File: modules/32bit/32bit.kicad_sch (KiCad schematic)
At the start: 19 parts, among them J5 USB_C_Receptacle_USB2.0_14P, SW1 K2-1808SN-A4SW-01, SW2 K2-1808SN-A4SW-01, U1 ESP32-S3-WROOM-1U-N16R8

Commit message: Add 32bit schematics
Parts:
- removed INPUT2: Conn_01x02_Socket, Connector_PinSocket_2.54mm:PinSocket_1x02_P2.54mm_Vertical, symbol Connector:Conn_01x02_Socket
- removed V1: 3.3, symbol Simulation_SPICE:VDC
- removed V2: VSIN, symbol Simulation_SPICE:VSIN
- added C21, C22, C26, C34, C36, C39: 0.1uf, Capacitor_SMD:C_0402_1005Metric, symbol Device:C_Small
- added C27, C33, C35, C37, C38, C5: 10uf, Capacitor_SMD:C_0402_1005Metric, symbol Device:C_Small
- added C6: 0.1uf, Capacitor_SMD:C_0402_1005Metric, symbol Device:C
- added D1: LED, LED_SMD:LED_0603_1608Metric, symbol Device:LED
- added R1, R2, R9: 1k, Resistor_SMD:R_0402_1005Metric, symbol Device:R
- added R10, R12: 100k, Resistor_SMD:R_0402_1005Metric, symbol Device:R
- added R13, R17: 1k, Resistor_SMD:R_0402_1005Metric, symbol Device:R_Small
- added R14, R18, R26, R7, R8: 33, Resistor_SMD:R_0402_1005Metric, symbol Device:R_Small
- added R24, R25: 4.7k, Resistor_SMD:R_0402_1005Metric, symbol Device:R_Small
- added R5, R6: 1.5k, Resistor_SMD:R_0402_1005Metric, symbol Device:R_Small
- added RV1, RV2: 50k, BreadModular_Pots:Potentiometer_RV09, symbol Device:R_Potentiometer
- added SW4: K2-1808SN-A4SW-01, BreadModular_MISC:K2-1808SN-A4SW-01, symbol Switch:SW_SPST
- added U3: MCP6002-xSN, Package_SO:SOIC-8-1EP_3.9x4.9mm_P1.27mm_EP2.29x3mm, symbol Amplifier_Operational:MCP6002-xSN
- added U4: ~, Package_DFN_QFN:QFN-28-1EP_4x4mm_P0.45mm_EP2.4x2.4mm_ThermalVias, symbol BreadModular_Symbols:ES8388
- INPUT1: value Conn_01x08_Socket -> Conn_01x05_Socket; footprint Connector_PinSocket_2.54mm:PinSocket_1x08_P2.54mm_Vertical -> Connector_PinSocket_2.54mm:PinSocket_1x05_P2.54mm_Vertical; symbol Connector:Conn_01x08_Socket -> Connector:Conn_01x05_Socket
- OUTPUT1: value Conn_01x08_Socket -> Conn_01x05_Socket; symbol Connector:Conn_01x08_Socket -> Connector:Conn_01x05_Socket
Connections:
- net GND: now also C21.2, C22.2, C26.2, C27.1, C33.2, C34.2, C35.2, C36.2, C37.2, C38.2, C39.2, C5.2, C6.2, R9.1, RV1.1, RV2.1, SW4.1 (A), U3.4 (V-), U4.13 (HPGND), U4.18 (AGND), U4.26 (CE), U4.29 (Thermal_Vias), U4.4 (DGND)
- net LED_MODE: now reaches U1.11 (IO18)
- net LED_MODE: now also D1.2 (A)
- net BUTTON_MODE: now reaches U1.12 (IO8)
- net BUTTON_MODE: now also SW4.2 (B)
- net CV1: now reaches U1.17 (IO9)
- net CV1: now also INPUT1.4 (Pin_4), R10.2, U3.3 (+)
- net CV2: now reaches U1.18 (IO10)
- net CV2: now also INPUT1.5 (Pin_5), R12.2, U3.5 (+)
- net at U1.19 (IO11): now also R7.2
- net at U1.20 (IO12): now also R8.2
- net at U1.21 (IO13): now also R14.2
- net at U1.22 (IO14): now also R18.2
- net at U1.23 (IO21): now also R26.1
- net CDATA: now reaches U1.24 (IO47)
- net CDATA: now also R24.1, U4.27 (CDATA)
- net CCLK: now reaches U1.25 (IO48)
- net CCLK: now also R25.1, U4.28 (CCLK)
- net at U1.38 (IO2): now also R2.2
- net at U1.39 (IO1): now also R1.2
- net EN: no longer names the net of C3.2, C4.2, R3.2, SW2.2 (B), U1.3 (EN)
- net IO0: no longer names the net of SW1.2 (B), U1.27 (IO0)
- net IO15: no longer names the net of U1.8 (IO15)
- net IO15: no longer INPUT1.6 (Pin_6)
- net IO16: no longer names the net of U1.9 (IO16)
- net IO16: no longer INPUT1.7 (Pin_7)
- net IO17: no longer names the net of U1.10 (IO17)
- net IO17: no longer INPUT1.8 (Pin_8)
- net IO35: no longer names the net of U1.28 (IO35)
- net IO35: no longer OUTPUT1.8 (Pin_8)
- net IO36: no longer names the net of U1.29 (IO36)
- net IO36: no longer OUTPUT1.7 (Pin_7)
- net IO37: no longer names the net of U1.30 (IO37)
- net IO37: no longer OUTPUT1.6 (Pin_6)
- net IO38: no longer names the net of U1.31 (IO38)
- net IO38: no longer OUTPUT1.5 (Pin_5)
- net IO39: no longer names the net of U1.32 (IO39)
- net IO39: no longer OUTPUT1.4 (Pin_4)
- net IO4: no longer names the net of U1.4 (IO4)
- net IO4: no longer INPUT1.2 (Pin_2)
- net IO40: no longer names the net of U1.33 (IO40)
- net IO40: no longer OUTPUT1.3 (Pin_3)
- net IO41: no longer names the net of U1.34 (IO41)
- net IO41: no longer OUTPUT1.2 (Pin_2)
- net IO5: no longer names the net of U1.5 (IO5)
- net IO5: no longer INPUT1.3 (Pin_3)
- net IO6: no longer names the net of U1.6 (IO6)
- net IO6: no longer INPUT1.4 (Pin_4)
- net IO7: no longer names the net of U1.7 (IO7)
- net IO7: no longer INPUT1.5 (Pin_5)
- new net: D1.1 (K), R9.2
- new net: R13.2, U4.11 (ROUT1)
- new net: R6.2, RV2.3
- new net: R5.2, RV1.3
- new net: R5.1, U3.1, U3.2 (-)
- new net: R6.1, U3.6 (-), U3.7
- new net: C33.1, C34.1, U4.20 (VMID)
- new net: R17.2, U4.12 (LOUT1)
- new net: C27.2, U4.10 (VREF)
- new net: C35.1, C36.1, U4.19 (ADCVREF)
- new net +3V3: C21.1, C22.1, C26.1, C37.1, C38.1, C39.1, C5.1, C6.1, R10.1, R12.1, R24.2, R25.2, U3.8 (V+), U4.16 (HPVDD), U4.17 (AVDD), U4.2 (DVDD), U4.3 (PVDD)
- new net AIN_1: INPUT1.2 (Pin_2), U4.24 (LIN1)
- new net AIN_2: INPUT1.3 (Pin_3), U4.23 (RIN1)
- new net AOUT_1: OUTPUT1.2 (Pin_2), R17.1
- new net AOUT_2: OUTPUT1.3 (Pin_3), R13.1
- new net ASDOUT: R26.2, U4.8 (ASDOUT)
- new net BUFF_CV1: RV1.2
- new net BUFF_CV2: RV2.2
- new net DSDIN: R18.1, U4.6 (DSDIN)
- new net GOUT_1: OUTPUT1.4 (Pin_4), R1.1
- new net GOUT_2: OUTPUT1.5 (Pin_5), R2.1
- new net LRCK: R14.1, U4.7 (LRCK)
- new net MCLK: R7.1, U4.1 (MCLK)
- new net SCLK: R8.1, U4.5 (SCLK)
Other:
- note added: "## Audio Codec ES8388"
- note added: "## CV_IN 1.5k before the pot is to reduce the voltage goes to ADC since we need to do some attenuation."
- note added: "## Other IO"
- note added: "## Processing Unit ESP32"
- note added: "## USB-C Setup"
- moved on the sheet: C20, GND1, J5, R11, R4, V_SUPPLY1

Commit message: Finished basic routing
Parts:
- OUTPUT1: footprint Connector_PinSocket_2.54mm:PinSocket_1x08_P2.54mm_Vertical -> Connector_PinSocket_2.54mm:PinSocket_1x05_P2.54mm_Vertical
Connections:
- net V_SUPPLY is gone; now on net +3V3: C1.1, C2.1, R3.1, U1.2 (3V3), V_SUPPLY1.1 (Pin_1), V_SUPPLY1.2 (Pin_2), V_SUPPLY1.3 (Pin_3), V_SUPPLY1.4 (Pin_4), V_SUPPLY1.5 (Pin_5)
- net ASDOUT: now also R7.1; no longer R26.2
- net BUFF_CV1: now also U1.17 (IO9)
- net BUFF_CV2: now also U1.18 (IO10)
- net CCLK: now also R24.1, U4.27 (CDATA); no longer R25.1, U4.28 (CCLK)
- net CDATA: now also R25.1, U4.28 (CCLK); no longer R24.1, U4.27 (CDATA)
- net CV1: no longer U1.17 (IO9)
- net CV2: no longer U1.18 (IO10)
- net DSDIN: now also R14.1; no longer R18.1
- net LRCK: now also R8.1; no longer R14.1
- net MCLK: now also R26.2; no longer R7.1
- net SCLK: now also R18.1; no longer R8.1

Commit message: Add the production files
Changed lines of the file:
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@@
-	(wire
-		(pts
-			(xy 80.01 86.36) (xy 81.28 86.36)
-		)
-		(stroke
-			(width 0)
-			(type default)
-		)
-	)
 	(wire
 		(pts
@@
 	(wire
 		(pts
-			(xy 80.01 109.22) (xy 81.28 109.22)
-		)
-		(stroke
-			(width 0)
-			(type default)
-		)
-	)
-	(wire
-		(pts
-			(xy 80.01 83.82) (xy 81.28 83.82)
-		)
-		(stroke
-			(width 0)
-			(type default)
-		)
-	)
-	(wire
-		(pts
 			(xy 224.79 54.61) (xy 228.6 54.61)
 		)
@@
 	(wire
 		(pts
-			(xy 80.01 111.76) (xy 81.28 111.76)
-		)
-		(stroke
-			(width 0)
-			(type default)
-		)
-	)
-	(wire
-		(pts
 			(xy 539.75 36.83) (xy 542.29 36.83)
 		)
@@
 	(wire
 		(pts
-			(xy 114.3 71.12) (xy 111.76 71.12)
-		)
-		(stroke
-			(width 0)
-			(type default)
-		)
-	)
-	(wire
-		(pts
 			(xy 128.27 245.11) (xy 128.27 251.46)
 		)
@@
 	(wire
 		(pts
-			(xy 80.01 88.9) (xy 81.28 88.9)
-		)
-		(stroke
-			(width 0)
-			(type default)
-		)
-	)
-	(wire
-		(pts
 			(xy 134.62 246.38) (xy 134.62 255.27)
 		)
@@
 		)
 		(stroke
-			(width 0)
-			(type default)
-		)
-	)
-	(wire
-		(pts
-			(xy 80.01 81.28) (xy 81.28 81.28)
-		)
-		(stroke

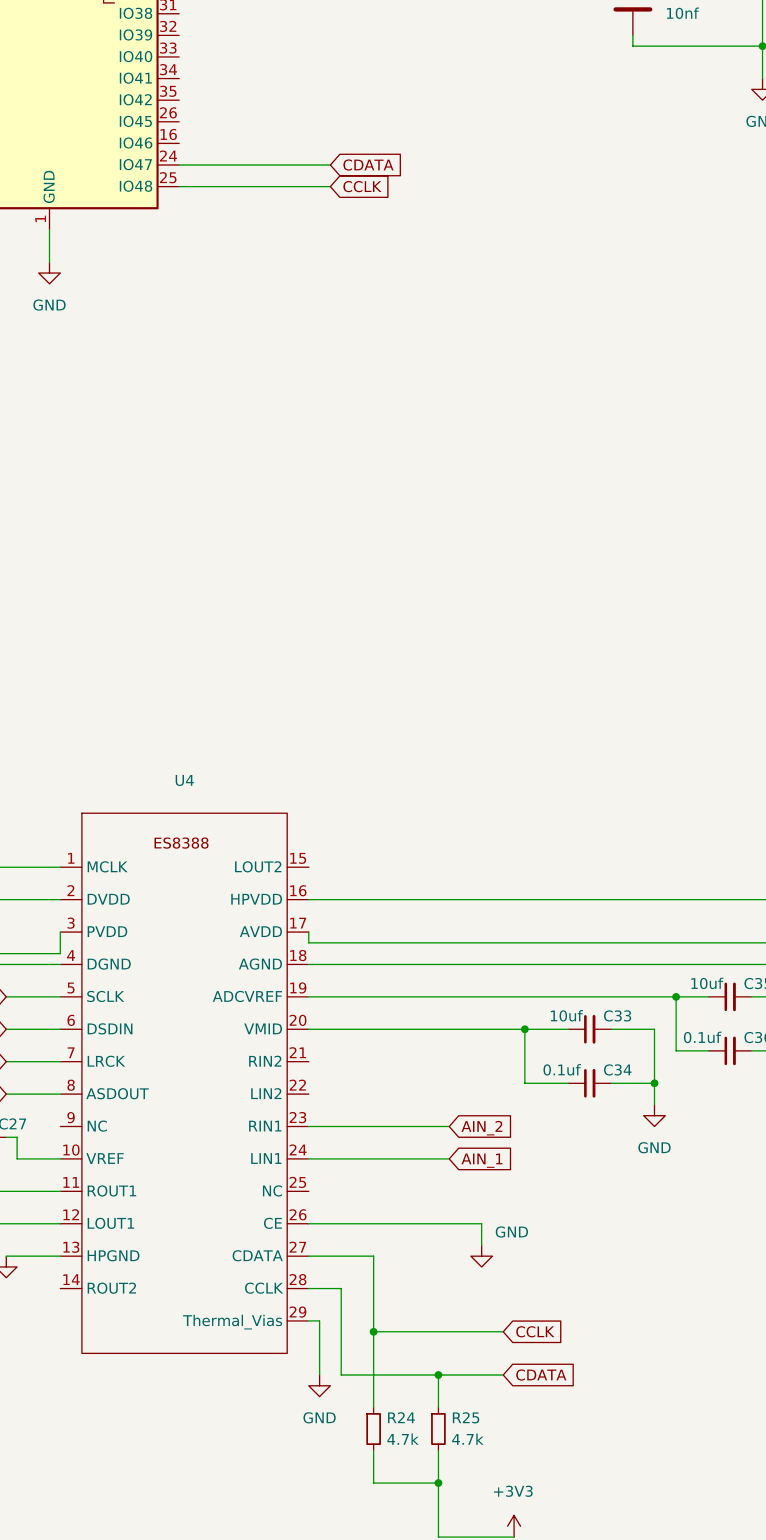
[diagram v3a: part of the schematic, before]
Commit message: 16bit: Moved CDATA & CCLK labels. They were just being marked wrongly in the ES8388 side
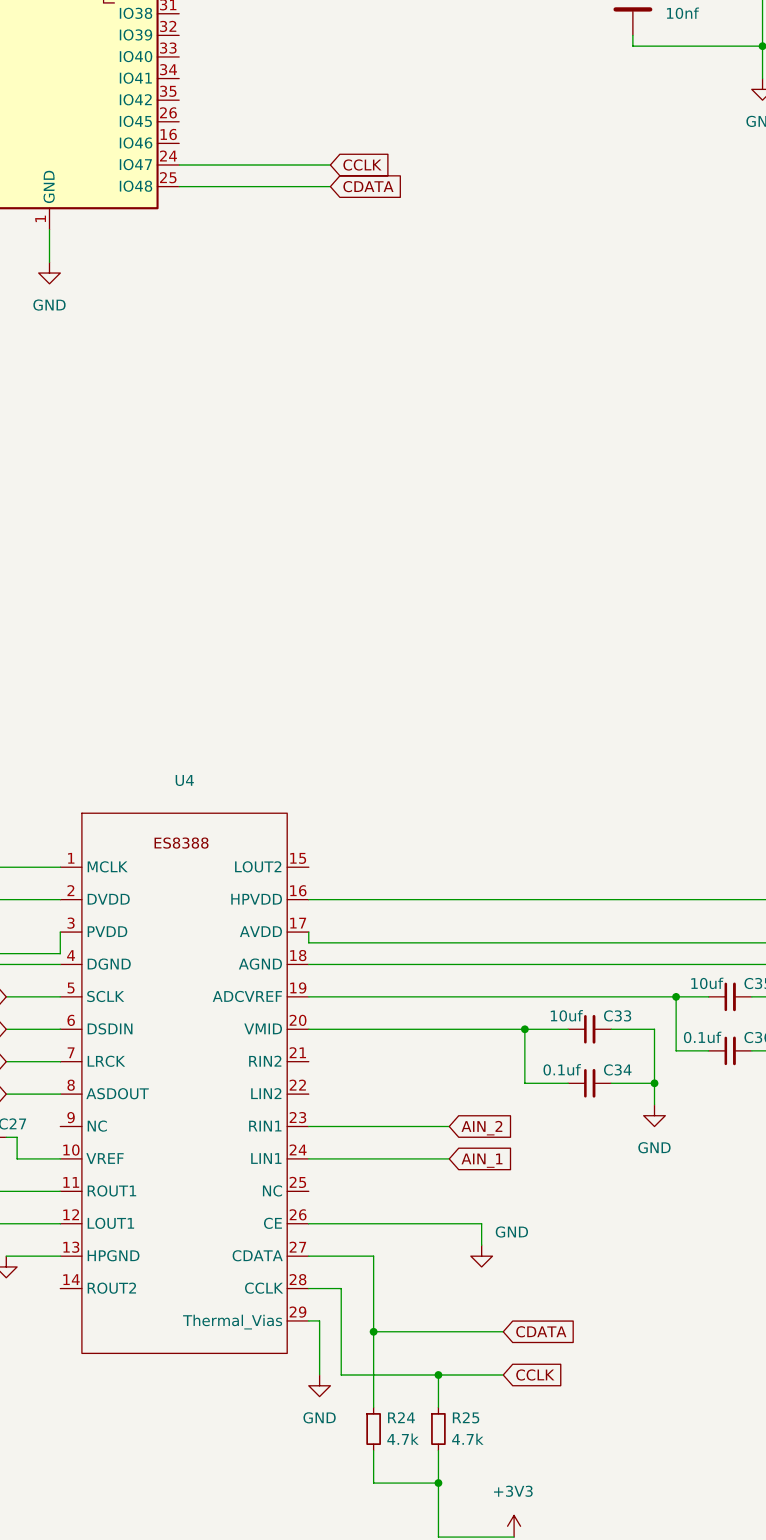
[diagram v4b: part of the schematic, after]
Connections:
- net CCLK: now also R25.1, U1.24 (IO47), U4.28 (CCLK); no longer R24.1, U1.25 (IO48), U4.27 (CDATA)
- net CDATA: now also R24.1, U1.25 (IO48), U4.27 (CDATA); no longer R25.1, U1.24 (IO47), U4.28 (CCLK)
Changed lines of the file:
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@@
 	)
 	(junction
+		(at 134.62 246.38)
+		(diameter 0)
+		(color 0 0 0 0)
+	)
+	(junction
 		(at 217.17 222.25)
 		(diameter 0)
@@
 	)
 	(junction
-		(at 134.62 246.38)
-		(diameter 0)
-		(color 0 0 0 0)
-	)
-	(junction
 		(at 506.73 38.1)
 		(diameter 0)
@@
 	)
 	(junction
-		(at 142.24 251.46)
-		(diameter 0)
-		(color 0 0 0 0)
-	)
-	(junction
 		(at 53.34 66.04)
 		(diameter 0)
@@
 		(color 0 0 0 0)
 	)
+	(junction
+		(at 142.24 251.46)
+		(diameter 0)
+		(color 0 0 0 0)
+	)
 	(wire
 		(pts
@@
 	(wire
 		(pts
-			(xy 142.24 251.46) (xy 149.86 251.46)
-		)
-		(stroke
-			(width 0)
-			(type default)
-		)
-	)
-	(wire
-		(pts
 			(xy 96.52 43.18) (xy 96.52 60.96)
 		)
@@
 	(wire
 		(pts
-			(xy 111.76 109.22) (xy 129.54 109.22)
+			(xy 33.02 307.34) (xy 48.26 307.34)
 		)
 		(stroke
@@
 	(wire
 		(pts
-			(xy 33.02 307.34) (xy 48.26 307.34)
+			(xy 116.84 311.15) (xy 116.84 309.88)
 		)
 		(stroke
@@
 	(wire
 		(pts
-			(xy 116.84 311.15) (xy 116.84 309.88)
+			(xy 127 233.68) (xy 147.32 233.68)
 		)
 		(stroke
@@
 	(wire
 		(pts
-			(xy 127 233.68) (xy 147.32 233.68)
+			(xy 111.76 109.22) (xy 129.54 109.22)
 		)
 		(stroke
@@
 	(wire
 		(pts
-			(xy 134.62 237.49) (xy 134.62 246.38)
-		)
-		(stroke
-			(width 0)
-			(type default)
-		)
-	)
-	(wire
-		(pts
 			(xy 91.44 218.44) (xy 97.79 218.44)
 		)
@@
 	(wire
 		(pts
+			(xy 134.62 246.38) (xy 134.62 255.27)
+		)
+		(stroke
+			(width 0)
+			(type default)
+		)
+	)
+	(wire
+		(pts
 			(xy 204.47 337.82) (xy 208.28 337.82)
 		)
@@
 	(wire
 		(pts
-			(xy 134.62 246.38) (xy 134.62 255.27)
+			(xy 134.62 237.49) (xy 134.62 246.38)
 		)
 		(stroke
@@
 	(wire
 		(pts
-			(xy 129.54 111.76) (xy 111.76 111.76)
-		)
-		(stroke
-			(width 0)
-			(type default)
-		)
-	)
-	(wire
-		(pts
 			(xy 33.02 346.71) (xy 33.02 347.98)
 		)
@@
 	(wire
 		(pts
+			(xy 134.62 246.38) (xy 149.86 246.38)
+		)
+		(stroke
+			(width 0)
+			(type default)
+		)
+	)
+	(wire
+		(pts
 			(xy 195.58 66.04) (xy 195.58 67.31)
 		)
@@
 	(wire
 		(pts
+			(xy 142.24 251.46) (xy 149.86 251.46)
+		)
+		(stroke
+			(width 0)
+			(type default)
+		)
+	)
+	(wire
+		(pts
 			(xy 58.42 229.87) (xy 97.79 229.87)
 		)
@@
 	(wire
 		(pts
-			(xy 248.92 222.25) (xy 217.17 222.25)
+			(xy 111.76 111.76) (xy 129.54 111.76)
 		)
 		(stroke
@@
 	(wire
 		(pts
-			(xy 58.42 233.68) (xy 97.79 233.68)
+			(xy 248.92 222.25) (xy 217.17 222.25)
 		)
 		(stroke
@@
 	(wire
 		(pts
-			(xy 29.21 83.82) (xy 22.86 83.82)
+			(xy 58.42 233.68) (xy 97.79 233.68)
 		)
 		(stroke
@@
 	(wire
 		(pts
-			(xy 76.2 223.52) (xy 86.36 223.52)
+			(xy 29.21 83.82) (xy 22.86 83.82)
 		)
 		(stroke
@@
 	(wire
 		(pts
-			(xy 30.48 107.95) (xy 30.48 110.49)
+			(xy 76.2 223.52) (xy 86.36 223.52)
 		)
 		(stroke
@@
 	(wire
 		(pts
-			(xy 134.62 246.38) (xy 149.86 246.38)
+			(xy 30.48 107.95) (xy 30.48 110.49)
 		)
 		(stroke
@@
 	(global_label "CDATA"
 		(shape input)
-		(at 129.54 109.22 0)
+		(at 129.54 111.76 0)
 		(fields_autoplaced yes)
 		(effects
@@
 		)
 		(property "Intersheetrefs" "${INTERSHEET_REFS}"
-			(at 138.21 109.22 0)
+			(at 138.21 111.76 0)
 			(effects
 				(font
@@
 	(global_label "CCLK"
 		(shape input)
-		(at 149.86 246.38 0)
+		(at 149.86 251.46 0)
 		(fields_autoplaced yes)
 		(effects
@@
 		)
 		(property "Intersheetrefs" "${INTERSHEET_REFS}"
-			(at 157.6833 246.38 0)
+			(at 157.6833 251.46 0)
 			(effects
 				(font
@@
 	(global_label "CCLK"
 		(shape input)
-		(at 129.54 111.76 0)
+		(at 129.54 109.22 0)
 		(fields_autoplaced yes)
 		(effects
@@
 		)
 		(property "Intersheetrefs" "${INTERSHEET_REFS}"
-			(at 137.3633 111.76 0)
+			(at 137.3633 109.22 0)
 			(effects
 				(font
@@
 	(global_label "CDATA"
 		(shape input)
-		(at 149.86 251.46 0)
+		(at 149.86 246.38 0)
 		(fields_autoplaced yes)
 		(effects
@@
 		)
 		(property "Intersheetrefs" "${INTERSHEET_REFS}"
-			(at 158.53 251.46 0)
+			(at 158.53 246.38 0)
 			(effects
 				(font

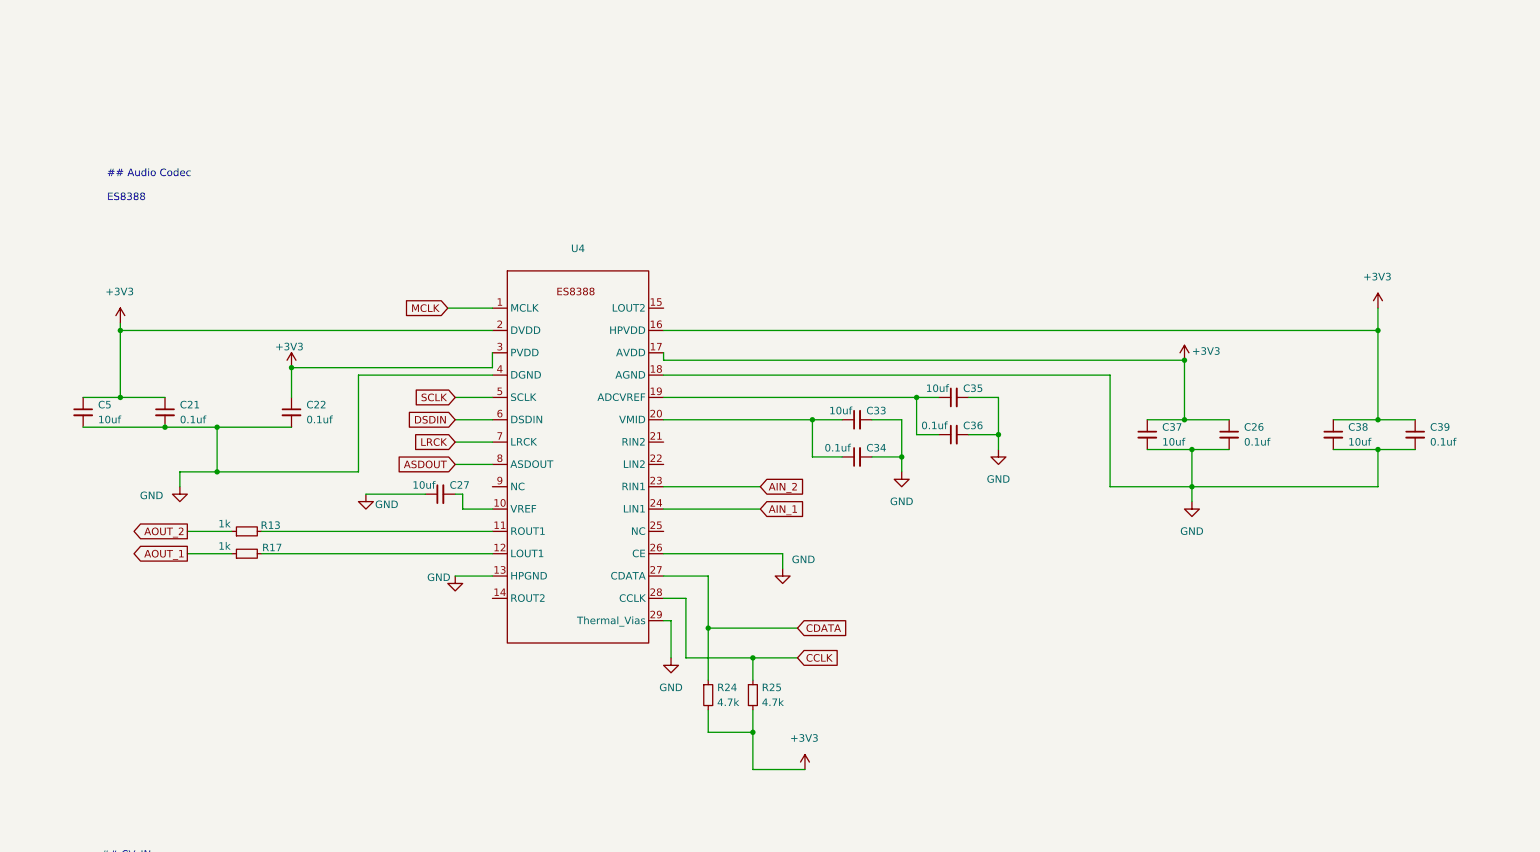
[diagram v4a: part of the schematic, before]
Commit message: Add a 3.3v island for es8388
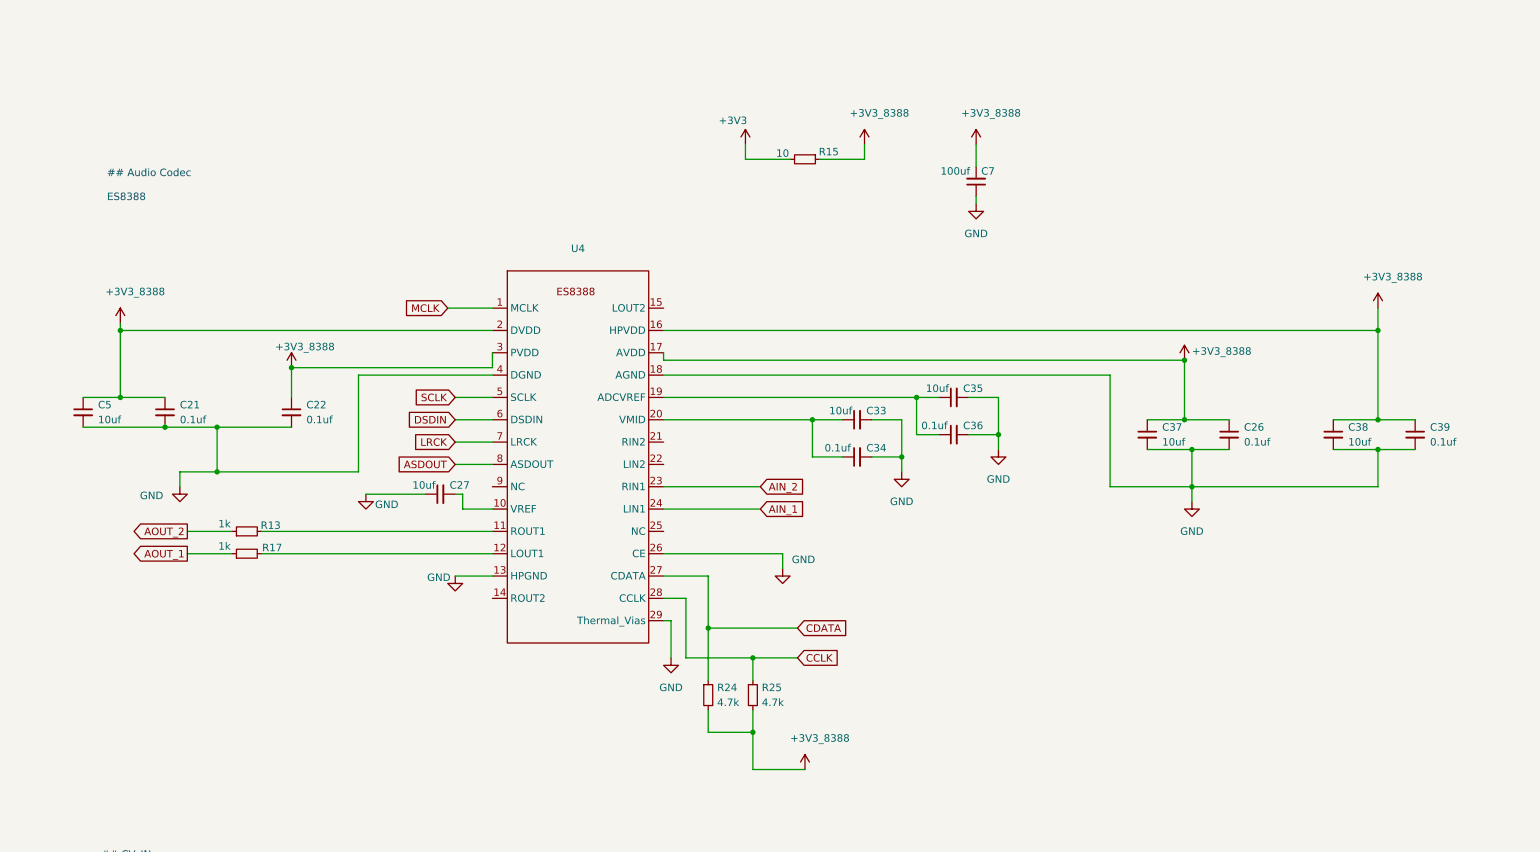
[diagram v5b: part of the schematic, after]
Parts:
- added C7: 100uf, Capacitor_SMD:C_1206_3216Metric, symbol Device:C_Small
- added R15: 10, Resistor_SMD:R_0603_1608Metric, symbol Device:R_Small
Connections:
- net +3V3: now also R15.2; no longer C21.1, C22.1, C26.1, C37.1, C38.1, C39.1, C5.1, R24.2, R25.2, U4.16 (HPVDD), U4.17 (AVDD), U4.2 (DVDD), U4.3 (PVDD)
- net GND: now also C7.1
- new net +3V3_8388: C21.1, C22.1, C26.1, C37.1, C38.1, C39.1, C5.1, C7.2, R15.1, R24.2, R25.2, U4.16 (HPVDD), U4.17 (AVDD), U4.2 (DVDD), U4.3 (PVDD)
